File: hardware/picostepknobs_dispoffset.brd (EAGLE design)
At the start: 177.8 x 81.3 mm, 56 parts, among them IC1 4051D, J1 AUDIO-JACK-TRRS, J2 AUDIO-JACK-TRRS, P1 10k, P2 10k, P3 10k, P4 10k, P5 10k, P6 10k, P7 10k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

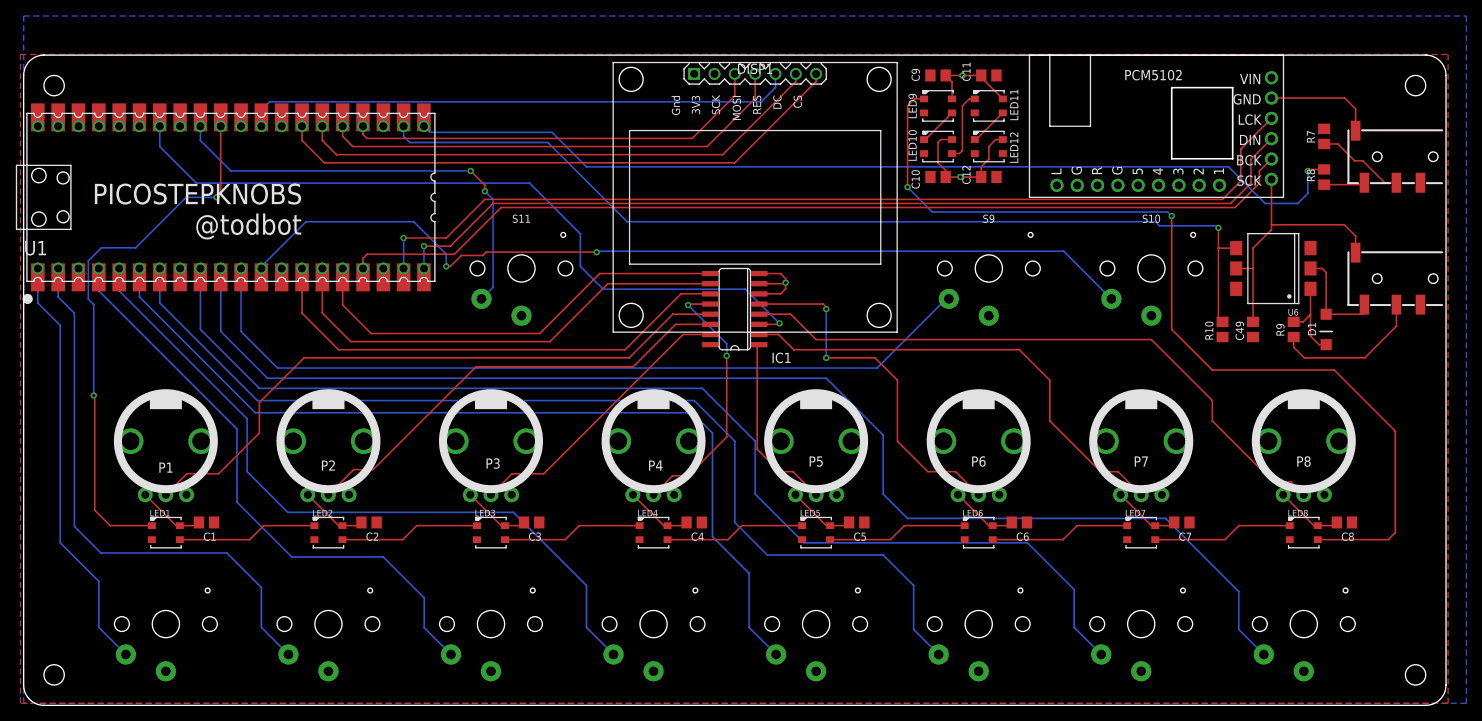
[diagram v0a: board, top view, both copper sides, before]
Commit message: brd: moved display to left
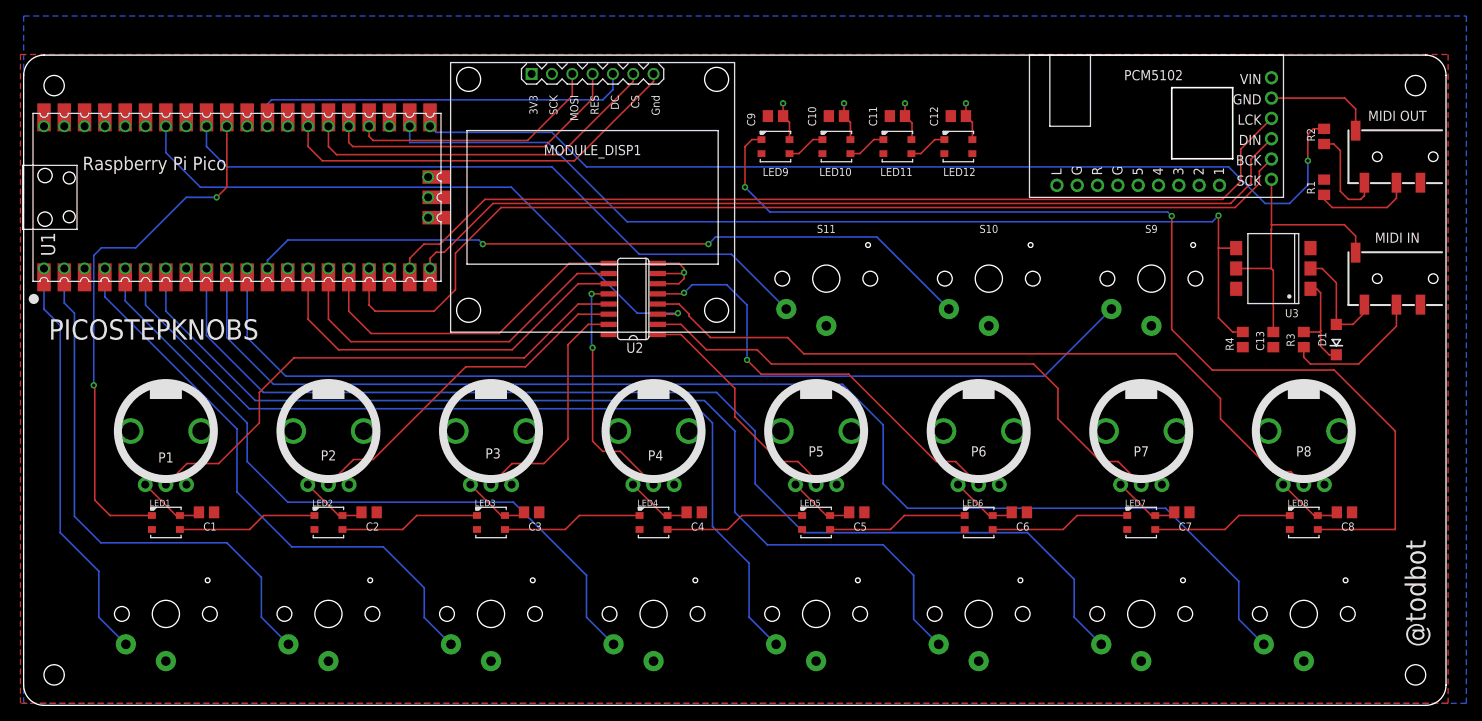
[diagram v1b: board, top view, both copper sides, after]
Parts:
- removed C49: 100n, rcl:C0805
- removed DISP1: DISPLAY-OLED-128X64-1.3IN, todstuff:DISPLAY-OLED-128X64-1.3IN
- removed IC1: 4051D, 40xx:SO16
- removed R10: 4.7k, rcl:R0805
- removed R8: 10, rcl:R0805
- removed R9: 220, rcl:R0805
- added C13: 100n, rcl:C0805
- added MODULE_DISP1: DISPLAY-OLED-128X64-1.3IN, todstuff2023:DISPLAY-OLED-128X64-1.3IN
- added R1: 33, rcl:R0805
- added R3: 220, rcl:R0805
- added R4: 4.7k, rcl:R0805
- added U2: 4051D, 40xx:SO16
- R2: value 33 -> 10
- U1: value PICO -> RASPBERRY_PICOSMD-TH; device RpiPico:PICO-PKG-NO_DEBUG -> RpiPico:PICO-PKG
- moved S11 38.1 mm to (100.3, 53.3)
- moved LED9 20.9 mm to (94.0, 69.8)
- moved C9 20.9 mm to (94.0, 73.7)
- moved S10 20.4 mm to (120.7, 53.3)
- moved S9 20.4 mm to (141.0, 53.3)
- moved C10 14.8 mm to (101.6, 73.7)
- moved LED10 12.7 mm to (101.6, 69.8)
- moved LED11 12.5 mm to (109.2, 69.8)
- moved C11 12.5 mm to (109.2, 73.7), turned to 0 degrees
- moved C12 8.52 mm to (116.8, 73.7), turned to 0 degrees
- moved LED12 3.81 mm to (116.8, 69.8)
- moved D1 1.80 mm to (164.1, 45.7)
- moved U1 1.37 mm to (26.7, 63.5)
- moved C1 1.27 mm to (22.9, 24.1)
- moved C2 1.27 mm to (43.2, 24.1)
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- renumbered PCM5102A to MODULE_PCM5102A, R7 to R2, U6 to U3
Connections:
- new net N$18: U1.41, U1.P$41
- new net N$19: U1.42, U1.P$42
- new net N$20: U1.43, U1.P$43
- net +3V3: now also C13.1, MODULE_DISP1.2, R1.2, R4.1, U2.16; no longer C49.1, DISP1.2, IC1.16, R10.1, R2.2
- net DISP_CS: now also MODULE_DISP1.7; no longer DISP1.7
- net DISP_DC: now also MODULE_DISP1.6; no longer DISP1.6
- net DISP_MOSI: now also MODULE_DISP1.4; no longer DISP1.4
- net DISP_RES: now also MODULE_DISP1.5; no longer DISP1.5
- net DISP_SCLK: now also MODULE_DISP1.3; no longer DISP1.3
- net GND: now also C13.2, MODULE_DISP1.1, U2.6, U2.7, U2.8; no longer C49.2, DISP1.1, IC1.6, IC1.7, IC1.8
- net MIDI_IN: now also R4.2; no longer R10.2
- net MIDI_OUT: now also R2.2; no longer R8.2
- net N$38: now also R1.1; no longer R2.1
- net N$47: now also R3.1; no longer R9.1
- net N$49: now also R3.2; no longer R9.2
- net N$9: now also R2.1; no longer R8.1
- net POT1: now also U2.13; no longer IC1.13
- net POT2: now also U2.14; no longer IC1.14
- net POT3: now also U2.15; no longer IC1.15
- net POT4: now also U2.12; no longer IC1.12
- net POT5: now also U2.1; no longer IC1.1
- net POT6: now also U2.5; no longer IC1.5
- net POT7: now also U2.2; no longer IC1.2
- net POT8: now also U2.4; no longer IC1.4
- net POTSELA: now also U2.11; no longer IC1.11
- net POTSELB: now also U2.10; no longer IC1.10
- net POTSELC: now also U2.9; no longer IC1.9
- net POT_IN: now also U2.3; no longer IC1.3
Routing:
- net SW11: track 56.0 -> 84.5 mm, vias 2 -> 0
- net SW10: track 116.4 -> 92.7 mm
- net DISP_CS: track 73.5 -> 52.6 mm
- net DISP_DC: track 67.5 -> 46.9 mm
- net DISP_MOSI: track 60.0 -> 39.4 mm
- net DISP_RES: track 70.3 -> 49.8 mm
- net SW9: track 102.9 -> 123.3 mm
- net DISP_SCLK: track 53.8 -> 34.1 mm
- net POT_IN: track 95.2 -> 79.3 mm
- net N$17: track 117.2 -> 131.7 mm
- net POT8: track 78.9 -> 91.7 mm
- net POT2: track 56.6 -> 43.9 mm
- net POT1: track 79.6 -> 66.9 mm
- net POTSELC: track 55.1 -> 42.6 mm
- net POTSELB: track 58.5 -> 46.1 mm
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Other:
- board text added: "- Raspberry Pi Pico - PCM5102 I2S stereo DAC - SH1106 1.3" SPI OLED - HL11L1 optoisolator - SK6812/WS2812 3535 SMD RGB LEDs - Choc keyswitches - Bournes PTV09A-4020 or Alps/Alpha pots - PJ320 TRRS jacks"
- board text added: "15 May 2023"
- board text added: "MIDI IN"
- board text added: "MIDI OUT"
- board text added: "Raspberry Pi Pico"
- board text added: "github.com/todbot/picostepknobs"
- board text added: "picostepknobs_dispoffset.brd"

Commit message: fix oled display helper notes on silkscreen
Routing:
- net DISP_RES: track 49.8 -> 54.8 mm
- net DISP_DC: track 46.9 -> 49.9 mm
- net DISP_CS: track 52.6 -> 55.6 mm
- net DISP_SCLK: track 34.1 -> 36.1 mm
- net DISP_MOSI: track 39.4 -> 41.2 mm
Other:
- board text added: "19 May 2023"
- board text removed: "15 May 2023"

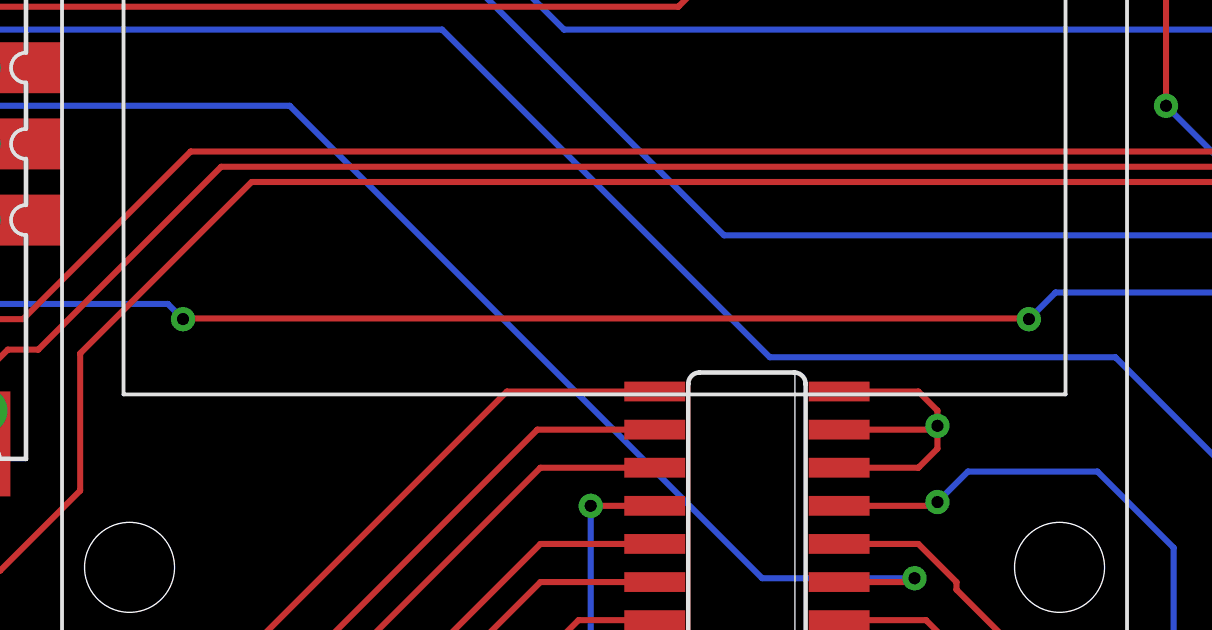
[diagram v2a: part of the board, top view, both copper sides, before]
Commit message: oops forgot bypass cap on 4051
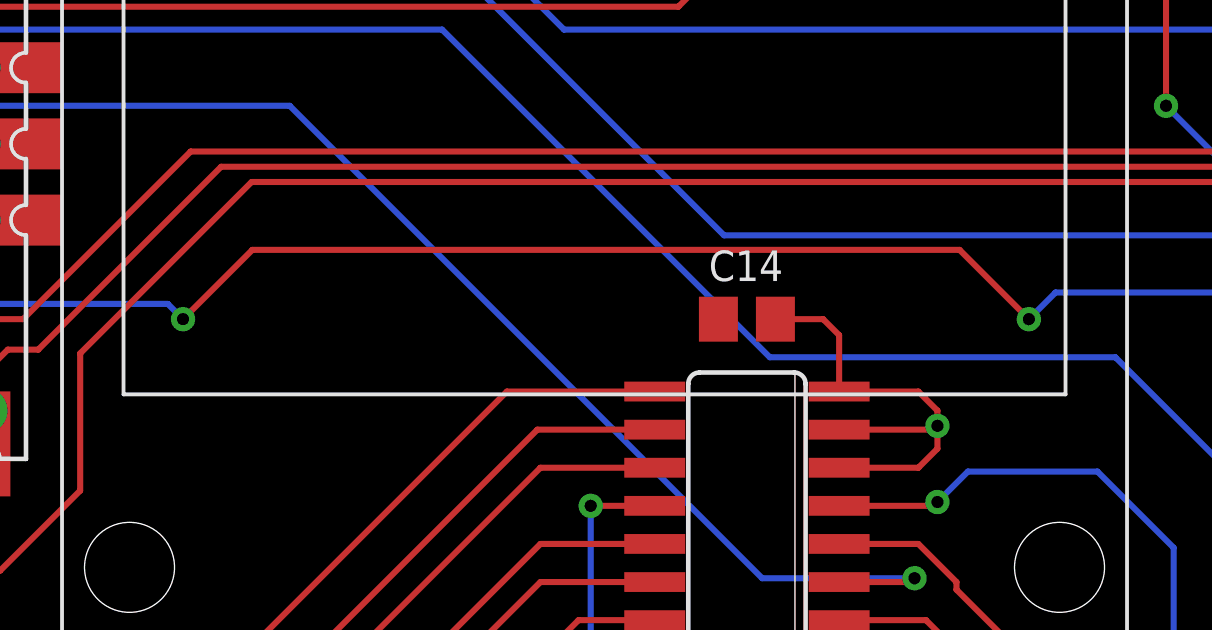
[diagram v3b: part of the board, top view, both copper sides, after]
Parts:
- added C14: 100n, rcl:C0805
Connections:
- net +3V3: now also C14.1
- net GND: now also C14.2
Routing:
- net GND: track 158.4 -> 162.6 mm
- net SW10: track 92.7 -> 94.6 mm
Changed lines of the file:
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@@
 <layer number="19" name="Unrouted" color="6" fill="1" visible="yes" active="yes"/>
 <layer number="20" name="Dimension" color="15" fill="1" visible="yes" active="yes"/>
-<layer number="21" name="tPlace" color="7" fill="1" visible="no" active="yes"/>
+<layer number="21" name="tPlace" color="7" fill="1" visible="yes" active="yes"/>
 <layer number="22" name="bPlace" color="7" fill="1" visible="yes" active="yes"/>
-<layer number="23" name="tOrigins" color="15" fill="1" visible="no" active="yes"/>
+<layer number="23" name="tOrigins" color="15" fill="1" visible="yes" active="yes"/>
 <layer number="24" name="bOrigins" color="15" fill="1" visible="yes" active="yes"/>
-<layer number="25" name="tNames" color="7" fill="1" visible="no" active="yes"/>
+<layer number="25" name="tNames" color="7" fill="1" visible="yes" active="yes"/>
 <layer number="26" name="bNames" color="7" fill="1" visible="yes" active="yes"/>
 <layer number="27" name="tValues" color="7" fill="1" visible="no" active="yes"/>
@@
 <layer number="37" name="tTest" color="7" fill="1" visible="no" active="yes"/>
 <layer number="38" name="bTest" color="7" fill="1" visible="no" active="yes"/>
-<layer number="39" name="tKeepout" color="4" fill="11" visible="no" active="yes"/>
+<layer number="39" name="tKeepout" color="4" fill="11" visible="yes" active="yes"/>
 <layer number="40" name="bKeepout" color="1" fill="11" visible="yes" active="yes"/>
-<layer number="41" name="tRestrict" color="4" fill="10" visible="no" active="yes"/>
+<layer number="41" name="tRestrict" color="4" fill="10" visible="yes" active="yes"/>
 <layer number="42" name="bRestrict" color="1" fill="10" visible="yes" active="yes"/>
 <layer number="43" name="vRestrict" color="2" fill="10" visible="no" active="yes"/>
 <layer number="44" name="Drills" color="7" fill="1" visible="no" active="yes"/>
-<layer number="45" name="Holes" color="7" fill="1" visible="no" active="yes"/>
+<layer number="45" name="Holes" color="7" fill="1" visible="yes" active="yes"/>
 <layer number="46" name="Milling" color="3" fill="1" visible="no" active="yes"/>
-<layer number="47" name="Measures" color="7" fill="1" visible="no" active="yes"/>
-<layer number="48" name="Document" color="7" fill="1" visible="no" active="yes"/>
-<layer number="49" name="Reference" color="7" fill="1" visible="no" active="yes"/>
+<layer number="47" name="Measures" color="7" fill="1" visible="yes" active="yes"/>
+<layer number="48" name="Document" color="7" fill="1" visible="yes" active="yes"/>
+<layer number="49" name="Reference" color="7" fill="1" visible="yes" active="yes"/>
 <layer number="50" name="dxf" color="7" fill="1" visible="no" active="no"/>
-<layer number="51" name="tDocu" color="7" fill="1" visible="no" active="yes"/>
+<layer number="51" name="tDocu" color="7" fill="1" visible="yes" active="yes"/>
 <layer number="52" name="bDocu" color="7" fill="1" visible="yes" active="yes"/>
 <layer number="53" name="tGND_GNDA" color="7" fill="9" visible="no" active="no"/>
@@
 <layer number="114" name="Panel" color="11" fill="1" visible="no" active="yes"/>
 <layer number="115" name="ReferenceISLANDS" color="7" fill="1" visible="no" active="yes"/>
-<layer number="116" name="Patch_BOT" color="9" fill="4" visible="no" active="yes"/>
+<layer number="116" name="Patch_BOT" color="9" fill="4" visible="yes" active="yes"/>
 <layer number="117" name="BACKMAAT1" color="7" fill="1" visible="no" active="yes"/>
 <layer number="118" name="Rect_Pads" color="7" fill="1" visible="no" active="yes"/>
@@
 <layer number="196" name="mValues" color="7" fill="1" visible="no" active="yes"/>
 <layer number="199" name="Contour" color="7" fill="1" visible="no" active="yes"/>
-<layer number="200" name="200bmp" color="1" fill="10" visible="no" active="yes"/>
-<layer number="201" name="201bmp" color="2" fill="10" visible="no" active="yes"/>
-<layer number="202" name="202bmp" color="3" fill="10" visible="no" active="yes"/>
+<layer number="200" name="200bmp" color="1" fill="10" visible="yes" active="yes"/>
+<layer number="201" name="201bmp" color="2" fill="10" visible="yes" active="yes"/>
+<layer number="202" name="202bmp" color="3" fill="10" visible="yes" active="yes"/>
 <layer number="203" name="203bmp" color="4" fill="10" visible="no" active="yes"/>
 <layer number="204" name="204bmp" color="5" fill="10" visible="no" active="yes"/>
@@
 <layer number="206" name="206bmp" color="7" fill="10" visible="no" active="yes"/>
 <layer number="207" name="207bmp" color="8" fill="10" visible="no" active="yes"/>
-<layer number="208" name="208bmp" color="9" fill="10" visible="no" active="yes"/>
-<layer number="209" name="209bmp" color="7" fill="1" visible="no" active="yes"/>
+<layer number="208" name="208bmp" color="9" fill="10" visible="yes" active="yes"/>
+<layer number="209" name="209bmp" color="7" fill="1" visible="yes" active="yes"/>
 <layer number="210" name="210bmp" color="7" fill="1" visible="no" active="yes"/>
 <layer number="211" name="211bmp" color="7" fill="1" visible="no" active="yes"/>
@@
 <attribute name="VALUE" x="71.12" y="45.99" size="1.27" layer="27" align="top-center"/>
 </element>
+<element name="C14" library="rcl" library_urn="urn:adsk.eagle:library:334" package="C0805" package3d_urn="urn:adsk.eagle:package:23617/2" value="100n" x="76.2" y="57.658" smashed="yes">
+<attribute name="NAME" x="74.93" y="58.928" size="1.016" layer="25" ratio="10"/>
+<attribute name="POPULARITY" value="88" x="76.2" y="57.658" size="1.778" layer="27" ratio="10" display="off"/>
+<attribute name="SPICEPREFIX" value="C" x="76.2" y="57.658" size="1.778" layer="27" ratio="10" display="off"/>
+<attribute name="VALUE" x="74.93" y="55.118" size="1.27" layer="27"/>
+</element>
 </elements>
 <signals>
@@
 <wire x1="82.423" y1="53.975" x2="82.55" y2="54.102" width="0.2032" layer="1"/>
 <contactref element="MODULE_DISP1" pad="1"/>
+<contactref element="C14" pad="2"/>
+<wire x1="77.15" y1="57.658" x2="78.74" y2="57.658" width="0.2032" layer="1"/>
+<wire x1="78.74" y1="57.658" x2="79.2734" y2="57.1246" width="0.2032" layer="1"/>
+<wire x1="79.2734" y1="57.1246" x2="79.2734" y2="55.245" width="0.2032" layer="1"/>
 </signal>
 <signal name="+3V3">
@@
 <contactref element="U1" pad="36"/>
 <contactref element="MODULE_DISP1" pad="2"/>
+<contactref element="C14" pad="1"/>
 </signal>
 <signal name="MIDI_OUT">
@@
 <wire x1="56.896" y1="58.166" x2="33.02" y2="58.166" width="0.2032" layer="16"/>
 <via x="57.404" y="57.658" extent="1-16" drill="0.4064"/>
-<wire x1="85.598" y1="57.658" x2="85.5744" y2="57.6816" width="0.2032" layer="1"/>
-<wire x1="85.5744" y1="57.6816" x2="57.4276" y2="57.6816" width="0.2032" layer="1"/>
-<wire x1="57.404" y1="57.658" x2="57.4276" y2="57.6816" width="0.2032" layer="1"/>
+<wire x1="85.598" y1="57.658" x2="83.2884" y2="59.9676" width="0.2032" layer="1"/>
+<wire x1="83.2884" y1="59.9676" x2="59.7136" y2="59.9676" width="0.2032" layer="1"/>
+<wire x1="57.404" y1="57.658" x2="59.7136" y2="59.9676" width="0.2032" layer="1"/>
 <contactref element="U1" pad="12"/>
 <contactref element="U1" pad="P$12"/>

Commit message: it is working a little
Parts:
- LED1, LED10, LED11, LED12, LED2, LED3, LED4, LED5, LED6, LED7, LED8, LED9: value WS2812B3535 -> WS2812B5050; device todstuff2023:LED3535 -> todstuff2023:WS2812B
- moved LED1 19.1 mm to (17.8, 3.81), turned to 270 degrees
- moved LED2 19.1 mm to (38.1, 3.81)
- moved LED3 19.1 mm to (58.4, 3.81)
- moved LED4 19.1 mm to (78.7, 3.81)
- moved LED5 19.1 mm to (99.1, 3.81)
- moved LED6 19.1 mm to (119.4, 3.81)
- moved LED7 19.1 mm to (139.7, 3.81)
- moved LED8 19.1 mm to (160.0, 3.81)
- moved C1 19.0 mm to (22.9, 5.08), turned to 90 degrees
- moved C2 19.0 mm to (43.2, 5.08)
- moved C3 19.0 mm to (63.5, 5.08)
- moved C4 19.0 mm to (83.8, 5.08)
- moved C5 19.0 mm to (104.1, 5.08)
- moved C6 19.0 mm to (124.5, 5.08)
- moved C7 19.0 mm to (144.8, 5.08)
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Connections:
- net +3V3: now also LED1.1-VDD, LED10.1-VDD, LED11.1-VDD, LED12.1-VDD, LED2.1-VDD, LED3.1-VDD, LED4.1-VDD, LED5.1-VDD, LED6.1-VDD, LED7.1-VDD, LED8.1-VDD, LED9.1-VDD; no longer LED1.2, LED10.2, LED11.2, LED12.2, LED2.2, LED3.2, LED4.2, LED5.2, LED6.2, LED7.2, LED8.2, LED9.2
- net GND: now also LED1.3-GND, LED10.3-GND, LED11.3-GND, LED12.3-GND, LED2.3-GND, LED3.3-GND, LED4.3-GND, LED5.3-GND, LED6.3-GND, LED7.3-GND, LED8.3-GND, LED9.3-GND; no longer LED1.4, LED10.4, LED11.4, LED12.4, LED2.4, LED3.4, LED4.4, LED5.4, LED6.4, LED7.4, LED8.4, LED9.4
- net N$1: now also LED1.2-DOUT, LED2.4-DIN; no longer LED1.3, LED2.1
- net N$10: now also LED4.2-DOUT, LED5.4-DIN; no longer LED4.3, LED5.1
- net N$11: now also LED5.2-DOUT, LED6.4-DIN; no longer LED5.3, LED6.1
- net N$12: now also LED6.2-DOUT, LED7.4-DIN; no longer LED6.3, LED7.1
- net N$13: now also LED7.2-DOUT, LED8.4-DIN; no longer LED7.3, LED8.1
- net N$14: now also LED10.4-DIN, LED9.2-DOUT; no longer LED10.1, LED9.3
- net N$15: now also LED10.2-DOUT, LED11.4-DIN; no longer LED10.3, LED11.1
- net N$16: now also LED11.2-DOUT, LED12.4-DIN; no longer LED11.3, LED12.1
- net N$17: now also LED8.2-DOUT, LED9.4-DIN; no longer LED8.3, LED9.1
- net N$2: now also LED2.2-DOUT, LED3.4-DIN; no longer LED2.3, LED3.1
- net N$4: now also LED3.2-DOUT, LED4.4-DIN; no longer LED3.3, LED4.1
- net NEOPIXEL: now also LED1.4-DIN; no longer LED1.1
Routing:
- net GND: track 162.6 -> 93.2 mm
- net NEOPIXEL: track 67.5 -> 86.2 mm
- net SW8: track 162.3 -> 144.5 mm
- net N$13: track 17.5 -> 0.00 mm
- net N$10: track 17.5 -> 0.00 mm
- net N$2: track 17.5 -> 0.00 mm
- net N$4: track 17.5 -> 0.00 mm
- net N$12: track 17.5 -> 0.00 mm
- net N$11: track 17.5 -> 0.00 mm
- net N$17: track 131.7 -> 119.6 mm
- net N$1: track 17.5 -> 11.9 mm
- net SW1: track 52.3 -> 47.3 mm
- net SW6: track 129.5 -> 124.4 mm
- net SW5: track 113.6 -> 108.5 mm
- net SW4: track 89.9 -> 84.8 mm
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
